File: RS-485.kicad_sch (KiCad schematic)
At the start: 16 parts, among them IC1 MAX485ESA+T

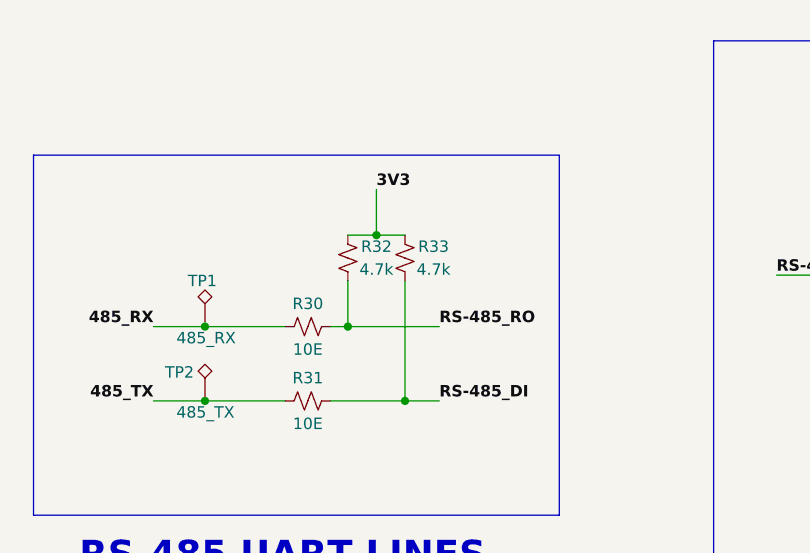
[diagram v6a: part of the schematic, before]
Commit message: Assigned footprints
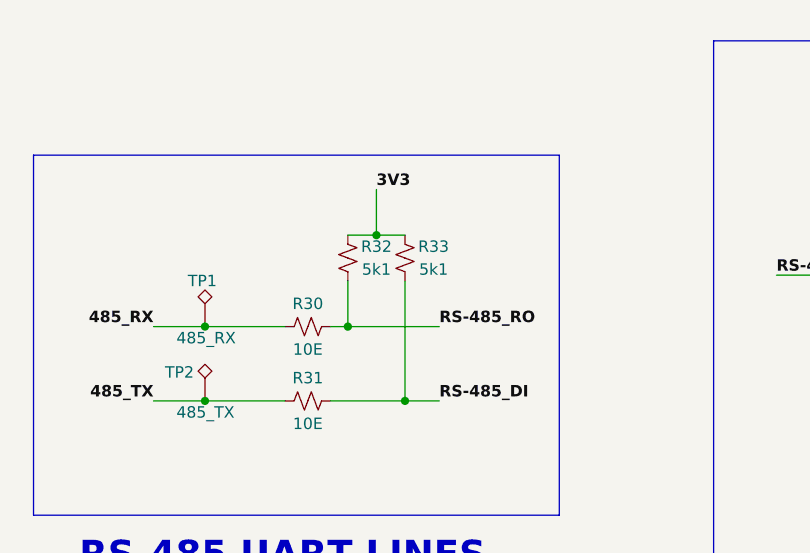
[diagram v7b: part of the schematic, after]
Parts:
- C22: footprint ESP32-S3_DB:C_0402_1005Metric -> ESP32-S3_Dev_Board:C_0402_1005Metric
- D6: footprint easyeda2kicad:SOT-23_L2.9-W1.3-P1.90-LS2.4-BR -> ESP32-S3_Dev_Board:SOT-23-3; PN (none) -> SM712
- IC1: footprint SOIC127P600X175-8N -> ESP32-S3_Dev_Board:SOP-8_3.9x4.9mm_P1.27mm; PN (none) -> MAX485ESA+T
- R13: footprint (none) -> ESP32-S3_Dev_Board:R_0603_1608Metric; PN (none) -> RC0603JR-070RL
- R24, R25, R30, R31: footprint (none) -> ESP32-S3_Dev_Board:R_0402_1005Metric; PN (none) -> RTT02100JTH
- R26: footprint (none) -> ESP32-S3_Dev_Board:R_0402_1005Metric; PN (none) -> RC0402FR-07120RL
- R27, R28, R29: footprint (none) -> ESP32-S3_Dev_Board:R_0402_1005Metric; PN (none) -> RC0402FR-0710KL
- R32, R33: value 4.7k -> 5k1; footprint (none) -> ESP32-S3_Dev_Board:R_0402_1005Metric; PN (none) -> RC0402FR-075K1L
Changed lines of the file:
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@@
       (effects (font (size 1.27 1.27)))
     )
-    (property "Footprint" "" (at 58.42 93.345 0)
+    (property "Footprint" "ESP32-S3_Dev_Board:R_0402_1005Metric" (at 58.42 93.345 0)
       (effects (font (size 1.27 1.27)) hide)
     )
@@
       (effects (font (size 1.27 1.27)) hide)
     )
+    (property "PN" "RTT02100JTH" (at 58.42 93.345 0)
+      (effects (font (size 1.27 1.27)) hide)
+    )
     (pin "1")
     (pin "2")
@@
       (effects (font (size 1.27 1.27)))
     )
-    (property "Footprint" "" (at 58.42 101.6 0)
+    (property "Footprint" "ESP32-S3_Dev_Board:R_0402_1005Metric" (at 58.42 101.6 0)
       (effects (font (size 1.27 1.27)) hide)
     )
@@
       (effects (font (size 1.27 1.27)) hide)
     )
+    (property "PN" "RTT02100JTH" (at 58.42 101.6 0)
+      (effects (font (size 1.27 1.27)) hide)
+    )
     (pin "1")
     (pin "2")
@@
       (effects (font (size 1.27 1.27)))
     )
-    (property "Footprint" "" (at 222.25 71.12 0)
+    (property "Footprint" "ESP32-S3_Dev_Board:R_0402_1005Metric" (at 222.25 71.12 0)
       (effects (font (size 1.27 1.27)) hide)
     )
@@
       (effects (font (size 1.27 1.27)) hide)
     )
+    (property "PN" "RTT02100JTH" (at 222.25 71.12 0)
+      (effects (font (size 1.27 1.27)) hide)
+    )
     (pin "1")
     (pin "2")
@@
       (effects (font (size 1.27 1.27)) (justify right))
     )
-    (property "Footprint" "" (at 235.585 75.565 0)
+    (property "Footprint" "ESP32-S3_Dev_Board:R_0402_1005Metric" (at 235.585 75.565 0)
       (effects (font (size 1.27 1.27)) hide)
     )
@@
       (effects (font (size 1.27 1.27)) hide)
     )
+    (property "PN" "RC0402FR-07120RL" (at 235.585 75.565 0)
+      (effects (font (size 1.27 1.27)) hide)
+    )
     (pin "1")
     (pin "2")
@@
       (effects (font (size 1.27 1.27)))
     )
-    (property "Footprint" "SOIC127P600X175-8N" (at 161.29 180.01 0)
+    (property "Footprint" "ESP32-S3_Dev_Board:SOP-8_3.9x4.9mm_P1.27mm" (at 161.29 180.01 0)
       (effects (font (size 1.27 1.27)) (justify left top) hide)
     )
@@
     (property "Arrow Price/Stock" "https://www.arrow.com/en/products/max485esat/maxim-integrated?region=nac" (at 161.29 1080.01 0)
       (effects (font (size 1.27 1.27)) (justify left top) hide)
+    )
+    (property "PN" "MAX485ESA+T" (at 139.7 85.09 0)
+      (effects (font (size 1.27 1.27)) hide)
     )
     (pin "1")
@@
       (effects (font (size 1.27 1.27)) (justify right))
     )
-    (property "Footprint" "" (at 242.57 66.675 0)
+    (property "Footprint" "ESP32-S3_Dev_Board:R_0402_1005Metric" (at 242.57 66.675 0)
       (effects (font (size 1.27 1.27)) hide)
     )
@@
       (effects (font (size 1.27 1.27)) hide)
     )
+    (property "PN" "RC0402FR-0710KL" (at 242.57 66.675 0)
+      (effects (font (size 1.27 1.27)) hide)
+    )
     (pin "1")
     (pin "2")
@@
       (effects (font (size 1.27 1.27)))
     )
-    (property "Footprint" "" (at 222.25 81.28 0)
+    (property "Footprint" "ESP32-S3_Dev_Board:R_0402_1005Metric" (at 222.25 81.28 0)
       (effects (font (size 1.27 1.27)) hide)
     )
@@
       (effects (font (size 1.27 1.27)) hide)
     )
+    (property "PN" "RTT02100JTH" (at 222.25 81.28 0)
+      (effects (font (size 1.27 1.27)) hide)
+    )
     (pin "1")
     (pin "2")
@@
       (effects (font (size 1.27 1.27)) (justify left))
     )
-    (property "Footprint" "" (at 165.1 76.2 0)
+    (property "Footprint" "ESP32-S3_Dev_Board:R_0603_1608Metric" (at 165.1 76.2 0)
       (effects (font (size 1.27 1.27)) hide)
     )
@@
       (effects (font (size 1.27 1.27)) hide)
     )
+    (property "PN" "RC0603JR-070RL" (at 165.1 76.2 0)
+      (effects (font (size 1.27 1.27)) hide)
+    )
     (pin "1")
     (pin "2")
@@
       (effects (font (size 1.27 1.27)) (justify right))
     )
-    (property "Footprint" "easyeda2kicad:SOT-23_L2.9-W1.3-P1.90-LS2.4-BR" (at 240.03 90.17 0)
+    (property "Footprint" "ESP32-S3_Dev_Board:SOT-23-3" (at 240.03 90.17 0)
       (effects (font (size 1.27 1.27)) hide)
     )
@@
       (effects (font (size 1.27 1.27)) hide)
     )
+    (property "PN" "SM712" (at 240.03 105.41 0)
+      (effects (font (size 1.27 1.27)) hide)
+    )
     (pin "1")
     (pin "2")
@@
       (effects (font (size 1.27 1.27)))
     )
-    (property "Value" "4.7k" (at 72.39 86.995 0)
-      (effects (font (size 1.27 1.27)))
-    )
-    (property "Footprint" "" (at 69.215 85.725 0)
+    (property "Value" "5k1" (at 72.39 86.995 0)
+      (effects (font (size 1.27 1.27)))
+    )
+    (property "Footprint" "ESP32-S3_Dev_Board:R_0402_1005Metric" (at 69.215 85.725 0)
       (effects (font (size 1.27 1.27)) hide)
     )
@@
       (effects (font (size 1.27 1.27)) hide)
     )
+    (property "PN" "RC0402FR-075K1L" (at 69.215 85.725 0)
+      (effects (font (size 1.27 1.27)) hide)
+    )
     (pin "1")
     (pin "2")
@@
       (effects (font (size 1.27 1.27)) (justify left))
     )
-    (property "Footprint" "ESP32-S3_DB:C_0402_1005Metric" (at 172.4152 78.105 0)
+    (property "Footprint" "ESP32-S3_Dev_Board:C_0402_1005Metric" (at 172.4152 78.105 0)
       (effects (font (size 1.27 1.27)) hide)
     )
@@
       (effects (font (size 1.27 1.27)))
     )
-    (property "Value" "4.7k" (at 66.04 86.995 0)
-      (effects (font (size 1.27 1.27)))
-    )
-    (property "Footprint" "" (at 62.865 85.725 0)
+    (property "Value" "5k1" (at 66.04 86.995 0)
+      (effects (font (size 1.27 1.27)))
+    )
+    (property "Footprint" "ESP32-S3_Dev_Board:R_0402_1005Metric" (at 62.865 85.725 0)
       (effects (font (size 1.27 1.27)) hide)
     )
@@
       (effects (font (size 1.27 1.27)) hide)
     )
+    (property "PN" "RC0402FR-075K1L" (at 62.865 85.725 0)
+      (effects (font (size 1.27 1.27)) hide)
+    )
     (pin "1")
     (pin "2")
@@
       (effects (font (size 1.27 1.27)) (justify right))
     )
-    (property "Footprint" "" (at 242.57 85.725 0)
+    (property "Footprint" "ESP32-S3_Dev_Board:R_0402_1005Metric" (at 242.57 85.725 0)
       (effects (font (size 1.27 1.27)) hide)
     )
@@
       (effects (font (size 1.27 1.27)) hide)
     )
+    (property "PN" "RC0402FR-0710KL" (at 242.57 85.725 0)
+      (effects (font (size 1.27 1.27)) hide)
+    )
     (pin "1")
     (pin "2")
@@
       (effects (font (size 1.27 1.27)) (justify right))
     )
-    (property "Footprint" "" (at 125.095 97.155 0)
+    (property "Footprint" "ESP32-S3_Dev_Board:R_0402_1005Metric" (at 125.095 97.155 0)
       (effects (font (size 1.27 1.27)) hide)
     )
@@
       (effects (font (size 1.27 1.27)) hide)
     )
+    (property "PN" "RC0402FR-0710KL" (at 125.095 97.155 0)
+      (effects (font (size 1.27 1.27)) hide)
+    )

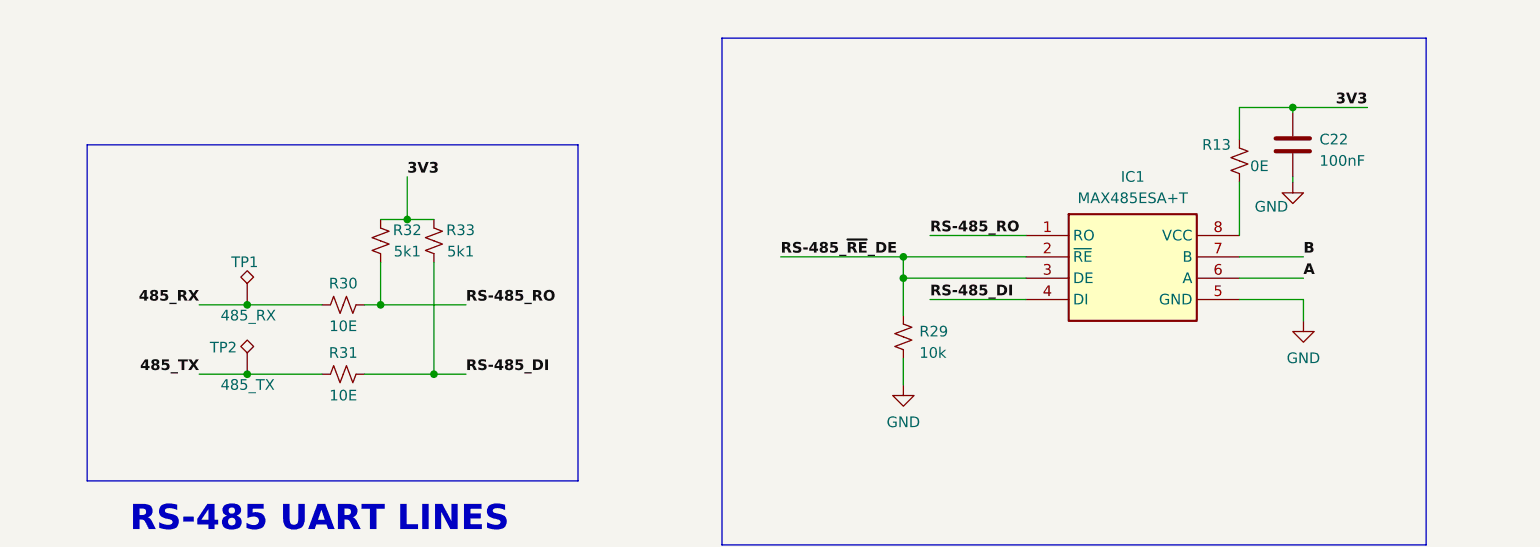
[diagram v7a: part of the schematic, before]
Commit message: Placed RS-485, CAN Transceiver and battery charger
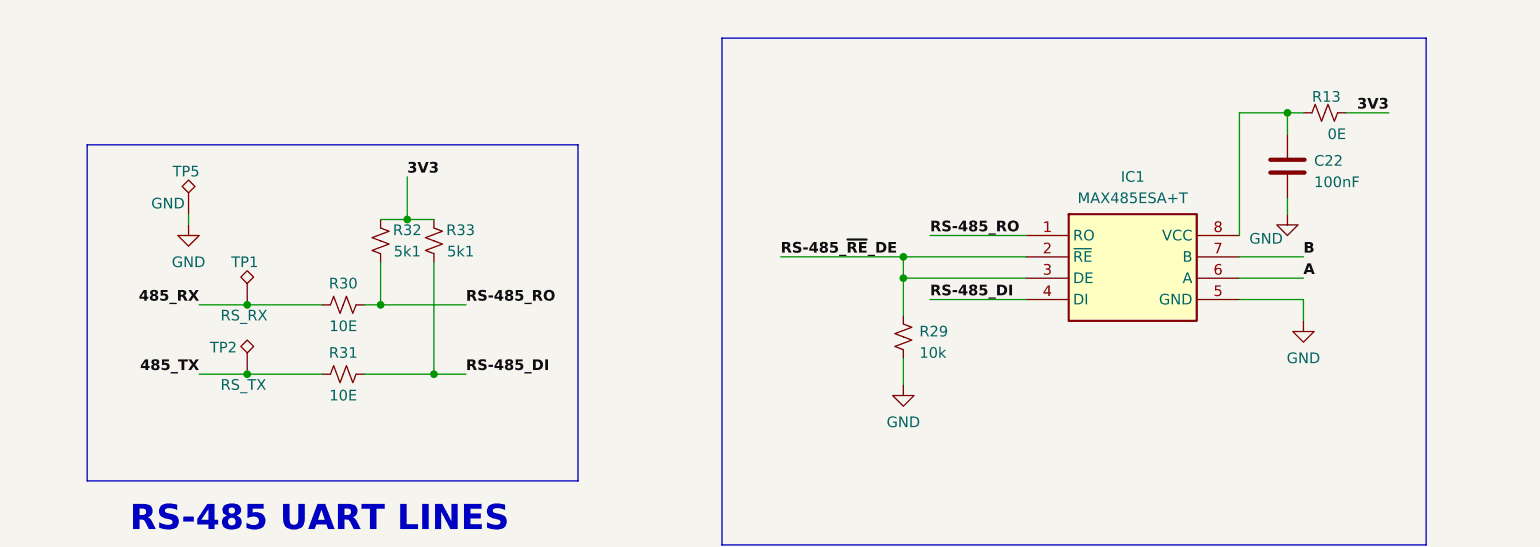
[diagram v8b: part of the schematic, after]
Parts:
- added TP5: GND, ESP32-S3_Dev_Board:Test_Pad_1.5mm, symbol ESP32-S3_DB:TestPoint_Alt
- TP1: value 485_RX -> RS_RX; footprint (none) -> ESP32-S3_Dev_Board:Test_Pad_1.5mm
- TP2: value 485_TX -> RS_TX; footprint (none) -> ESP32-S3_Dev_Board:Test_Pad_1.5mm
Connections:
- net 3V3: now also R13.2; no longer C22.1, R13.1
- net GND: now also TP5.1
- net at IC1.8 (VCC): now also C22.1, R13.1; no longer R13.2
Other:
- moved on the sheet: C22, R13
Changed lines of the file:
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@@
   (junction (at 66.04 83.185) (diameter 0) (color 0 0 0 0)
   )
+  (junction (at 170.815 70.485) (diameter 0) (color 0 0 0 0)
+  )
   (junction (at 235.585 81.28) (diameter 0) (color 0 0 0 0)
   )
-  (junction (at 171.45 69.85) (diameter 0) (color 0 0 0 0)
-  )
   (junction (at 125.095 90.17) (diameter 0) (color 0 0 0 0)
   )
@@
     (stroke (width 0) (type default))
   )
-  (wire (pts (xy 171.45 78.105) (xy 171.45 78.74))
+  (wire (pts (xy 170.815 80.645) (xy 170.815 82.55))
     (stroke (width 0) (type default))
   )
@@
     (stroke (width 0) (type default))
   )
-  (wire (pts (xy 165.1 69.85) (xy 171.45 69.85))
-    (stroke (width 0) (type default))
-  )
   (wire (pts (xy 125.095 94.615) (xy 125.095 90.17))
-    (stroke (width 0) (type default))
-  )
-  (wire (pts (xy 171.45 69.85) (xy 171.45 70.485))
     (stroke (width 0) (type default))
   )
@@
     (stroke (width 0) (type default))
   )
+  (wire (pts (xy 165.1 70.485) (xy 165.1 85.09))
+    (stroke (width 0) (type default))
+  )
   (wire (pts (xy 217.17 78.105) (xy 217.17 81.28))
     (stroke (width 0) (type default))
@@
     (stroke (width 0) (type default))
   )
+  (wire (pts (xy 177.8 70.485) (xy 182.88 70.485))
+    (stroke (width 0) (type default))
+  )
+  (wire (pts (xy 170.815 70.485) (xy 172.72 70.485))
+    (stroke (width 0) (type default))
+  )
   (bus (pts (xy 187.325 121.92) (xy 103.505 121.92))
     (stroke (width 1) (type default) (color 72 72 72 1))
@@
     (stroke (width 1) (type default) (color 72 72 72 1))
   )
+  (wire (pts (xy 170.815 70.485) (xy 165.1 70.485))
+    (stroke (width 0) (type default))
+  )
   (wire (pts (xy 242.57 90.17) (xy 242.57 88.265))
     (stroke (width 0) (type default))
@@
     (stroke (width 0) (type default))
   )
-  (wire (pts (xy 165.1 78.74) (xy 165.1 85.09))
-    (stroke (width 0) (type default))
-  )
   (wire (pts (xy 69.215 101.6) (xy 73.025 101.6))
     (stroke (width 0) (type default))
@@
     (stroke (width 0) (type default))
   )
-  (wire (pts (xy 165.1 69.85) (xy 165.1 73.66))
+  (wire (pts (xy 170.815 73.025) (xy 170.815 70.485))
     (stroke (width 0) (type default))
   )
@@
     (stroke (width 0) (type default))
   )
-  (wire (pts (xy 171.45 69.85) (xy 180.34 69.85))
-    (stroke (width 0) (type default))
-  )
   (bus (pts (xy 27.94 74.295) (xy 86.36 74.295))
     (stroke (width 1) (type default) (color 72 72 72 1))
+  )
+  (wire (pts (xy 40.005 83.82) (xy 40.005 82.55))
+    (stroke (width 0) (type default))
   )
   (wire (pts (xy 235.585 81.28) (xy 242.57 81.28))
@@
     (effects (font (size 1.27 1.27) (thickness 0.254) bold (color 0 0 0 1)) (justify left bottom))
   )
-  (label "3V3" (at 180.34 69.85 180) (fields_autoplaced)
+  (label "3V3" (at 182.88 70.485 180) (fields_autoplaced)
     (effects (font (size 1.27 1.27) (thickness 0.254) bold (color 255 0 0 1)) (justify right bottom))
   )
@@
     )
   )
-  (symbol (lib_id "ESP32-S3_DB:GND") (at 171.45 78.74 0) (unit 1)
-    (in_bom yes) (on_board yes) (dnp no)
-    (property "Reference" "#PWR035" (at 171.45 85.09 0)
-      (effects (font (size 1.27 1.27)) hide)
-    )
-    (property "Value" "GND" (at 168.91 81.661 0)
-      (effects (font (size 1.27 1.27)))
-    )
-    (property "Footprint" "" (at 171.45 78.74 0)
-      (effects (font (size 1.27 1.27)) hide)
-    )
-    (property "Datasheet" "" (at 171.45 78.74 0)
+  (symbol (lib_id "ESP32-S3_DB:GND") (at 170.815 82.55 0) (unit 1)
+    (in_bom yes) (on_board yes) (dnp no)
+    (property "Reference" "#PWR035" (at 170.815 88.9 0)
+      (effects (font (size 1.27 1.27)) hide)
+    )
+    (property "Value" "GND" (at 168.275 85.471 0)
+      (effects (font (size 1.27 1.27)))
+    )
+    (property "Footprint" "" (at 170.815 82.55 0)
+      (effects (font (size 1.27 1.27)) hide)
+    )
+    (property "Datasheet" "" (at 170.815 82.55 0)
       (effects (font (size 1.27 1.27)) hide)
     )
@@
       (effects (font (size 1.27 1.27)) (justify left))
     )
-    (property "Value" "485_TX" (at 43.815 102.87 0)
+    (property "Value" "RS_TX" (at 43.815 102.87 0)
       (effects (font (size 1.27 1.27)) (justify left))
     )
-    (property "Footprint" "" (at 52.07 101.6 0)
+    (property "Footprint" "ESP32-S3_Dev_Board:Test_Pad_1.5mm" (at 52.07 101.6 0)
       (effects (font (size 1.27 1.27)) hide)
     )
@@
     )
   )
-  (symbol (lib_id "ESP32-S3_DB:R_Small_US") (at 165.1 76.2 0) (unit 1)
-    (in_bom yes) (on_board yes) (dnp no)
-    (property "Reference" "R13" (at 160.655 74.295 0)
+  (symbol (lib_id "ESP32-S3_DB:R_Small_US") (at 175.26 70.485 90) (unit 1)
+    (in_bom yes) (on_board yes) (dnp no)
+    (property "Reference" "R13" (at 177.165 68.58 90)
       (effects (font (size 1.27 1.27)) (justify left))
     )
-    (property "Value" "0E" (at 166.37 76.835 0)
+    (property "Value" "0E" (at 177.8 73.025 90)
       (effects (font (size 1.27 1.27)) (justify left))
     )
-    (property "Footprint" "ESP32-S3_Dev_Board:R_0603_1608Metric" (at 165.1 76.2 0)
-      (effects (font (size 1.27 1.27)) hide)
-    )
-    (property "Datasheet" "~" (at 165.1 76.2 0)
-      (effects (font (size 1.27 1.27)) hide)
-    )
-    (property "PN" "RC0603JR-070RL" (at 165.1 76.2 0)
+    (property "Footprint" "ESP32-S3_Dev_Board:R_0603_1608Metric" (at 175.26 70.485 0)
+      (effects (font (size 1.27 1.27)) hide)
+    )
+    (property "Datasheet" "~" (at 175.26 70.485 0)
+      (effects (font (size 1.27 1.27)) hide)
+    )
+    (property "PN" "RC0603JR-070RL" (at 175.26 70.485 0)
       (effects (font (size 1.27 1.27)) hide)
     )
@@
     )
   )
-  (symbol (lib_id "ESP32-S3_DB:C") (at 171.45 74.295 0) (unit 1)
+  (symbol (lib_id "ESP32-S3_DB:C") (at 170.815 76.835 0) (unit 1)
     (in_bom yes) (on_board yes) (dnp no) (fields_autoplaced)
-    (property "Reference" "C22" (at 174.625 73.66 0)
+    (property "Reference" "C22" (at 173.99 76.2 0)
       (effects (font (size 1.27 1.27)) (justify left))
     )
-    (property "Value" "100nF" (at 174.625 76.2 0)
+    (property "Value" "100nF" (at 173.99 78.74 0)
       (effects (font (size 1.27 1.27)) (justify left))
     )
-    (property "Footprint" "ESP32-S3_Dev_Board:C_0402_1005Metric" (at 172.4152 78.105 0)
-      (effects (font (size 1.27 1.27)) hide)
-    )
-    (property "Datasheet" "~" (at 171.45 74.295 0)
-      (effects (font (size 1.27 1.27)) hide)
-    )
-    (property "PN" "EMK107B7104KAHT" (at 171.45 74.295 0)
+    (property "Footprint" "ESP32-S3_Dev_Board:C_0402_1005Metric" (at 171.7802 80.645 0)
+      (effects (font (size 1.27 1.27)) hide)
+    )
+    (property "Datasheet" "~" (at 170.815 76.835 0)
+      (effects (font (size 1.27 1.27)) hide)
+    )
+    (property "PN" "EMK107B7104KAHT" (at 170.815 76.835 0)
       (effects (font (size 1.27 1.27)) hide)
     )
@@
       (effects (font (size 1.27 1.27)) (justify left))
     )
-    (property "Value" "485_RX" (at 43.815 94.615 0)
+    (property "Value" "RS_RX" (at 43.815 94.615 0)
       (effects (font (size 1.27 1.27)) (justify left))
     )
-    (property "Footprint" "" (at 52.07 93.345 0)
+    (property "Footprint" "ESP32-S3_Dev_Board:Test_Pad_1.5mm" (at 52.07 93.345 0)
       (effects (font (size 1.27 1.27)) hide)
     )
@@
         )
       )
+    )
+  )
+  (symbol (lib_id "ESP32-S3_DB:TestPoint_Alt") (at 40.005 82.55 0) (unit 1)
+    (in_bom yes) (on_board yes) (dnp no)
+    (property "Reference" "TP5" (at 38.1 77.47 0)
+      (effects (font (size 1.27 1.27)) (justify left))
+    )
+    (property "Value" "GND" (at 35.56 81.28 0)
+      (effects (font (size 1.27 1.27)) (justify left))
+    )
+    (property "Footprint" "ESP32-S3_Dev_Board:Test_Pad_1.5mm" (at 45.085 82.55 0)
+      (effects (font (size 1.27 1.27)) hide)
+    )
+    (property "Datasheet" "~" (at 45.085 82.55 0)
+      (effects (font (size 1.27 1.27)) hide)
+    )
+    (pin "1")
+    (instances
+      (project "ESP32-S3_DB"
+        (path "/b7fc4bd3-c219-4455-832b-8d795385dcf1/9b4afe2f-79e5-4a56-98d7-d16b193c0e70"
+          (reference "TP5") (unit 1)
+        )
+      )
+    )
+  )
+  (symbol (lib_id "ESP32-S3_DB:GND") (at 40.005 83.82 0) (unit 1)
+    (in_bom yes) (on_board yes) (dnp no) (fields_autoplaced)
+    (property "Reference" "#PWR069" (at 40.005 90.17 0)
+      (effects (font (size 1.27 1.27)) hide)
+    )
+    (property "Value" "GND" (at 40.005 88.265 0)
+      (effects (font (size 1.27 1.27)))
+    )
+    (property "Footprint" "" (at 40.005 83.82 0)
+      (effects (font (size 1.27 1.27)) hide)
+    )
+    (property "Datasheet" "" (at 40.005 83.82 0)
+      (effects (font (size 1.27 1.27)) hide)
+    )
+    (pin "1")
+    (instances
+      (project "ESP32-S3_DB"
+        (path "/b7fc4bd3-c219-4455-832b-8d795385dcf1/9b4afe2f-79e5-4a56-98d7-d16b193c0e70"
+          (reference "#PWR069") (unit 1)
+        )
+      )
